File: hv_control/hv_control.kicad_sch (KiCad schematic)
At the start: 158 parts, among them J1 DB9, J10 x, J11 Conn_02x03_Odd_Even, J12 x, J13 Conn_01x02_Male, J14 Conn_01x02_Male, J15 Conn_01x02_Male, J16 Conn_01x02_Male, J17 Conn_01x02_Male, J2 DB15, J3 INPUTS, J4 I/O, J5 USB_B_Mini, J6 Conn_01x01_Male, J7 Conn_01x01_Male, J8 Conn_02x04_Odd_Even, J9 x, K1 RELAY_DPDT, K2 RELAY_DPDT, P2 SWD, P8 CONN_01X01, Q2 BSS138, Q3 BSS138, U1 XMC4400-F100, U10 XMC1301T016F0032ABXUMA1, U11 LT1764EQ, U12 LMV331, U13 DRV8870DDA, U14 AD8226, U15 MAX3463, U18 LT1764EQ, U19 KSZ8081, U2 ips511g, U20 ETH100_MAG, U21 MAX3463, U22 MAX3463, U23 MAX3463, U3 ips511g, U4 MAX3463, U5 AD8226, U6 R-78E5.0-0.5, U7 TS321, U8 R-78E3.3-0.5, U9 ISO7321C, Y1 12MHz, Y2 25MHz

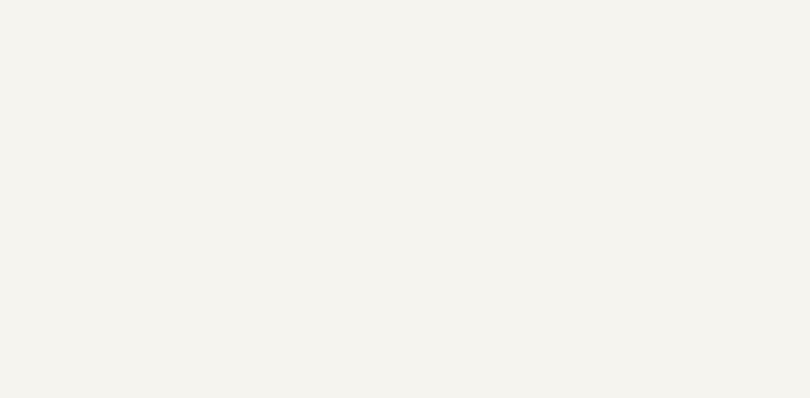
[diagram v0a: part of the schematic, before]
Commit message: Initial xmc1300 code.
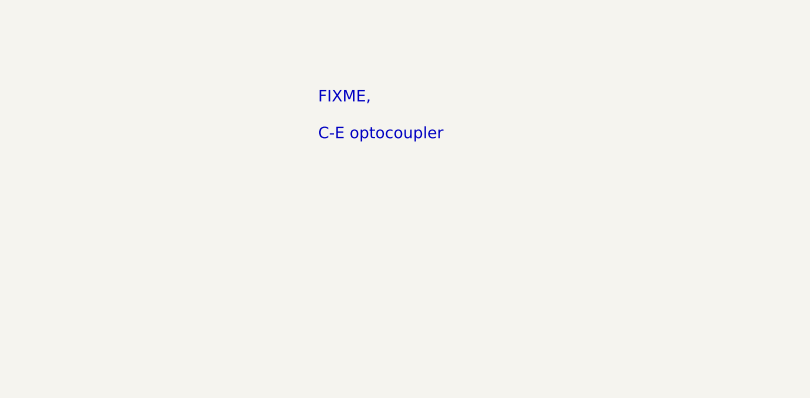
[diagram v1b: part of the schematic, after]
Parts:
- Y2: Mouser (none) -> 581-CX3225CA25000PPQ
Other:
- note added: "FIXME, C-E optocoupler"
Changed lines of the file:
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@@
     (effects (font (size 1.27 1.27)) (justify right bottom))
   )
+  (text "FIXME,\n\nC-E optocoupler" (at 400.05 29.21 0)
+    (effects (font (size 1.27 1.27)) (justify left bottom))
+  )
   (label "VddC" (at 45.72 370.84 0)
     (effects (font (size 1.524 1.524)) (justify left bottom))
@@
       (effects (font (size 1.27 1.27)) hide)
     )
+    (property "Mouser" " 581-CX3225CA25000PPQ " (id 8) (at 203.2 130.81 0)
+      (effects (font (size 1.27 1.27)) hide)
+    )

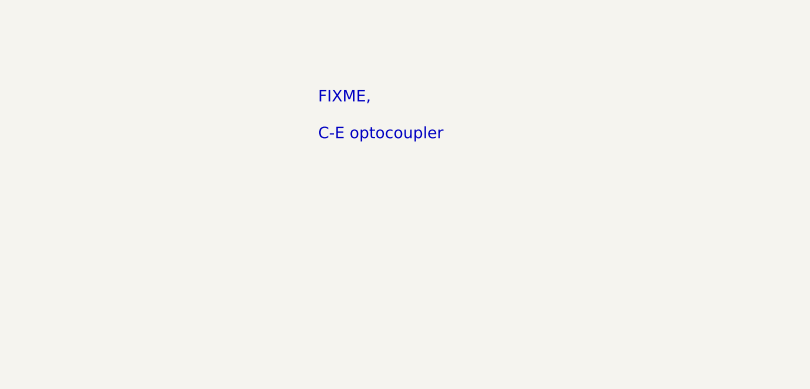
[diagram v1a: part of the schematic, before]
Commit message: xmc1300 can toggle pin.
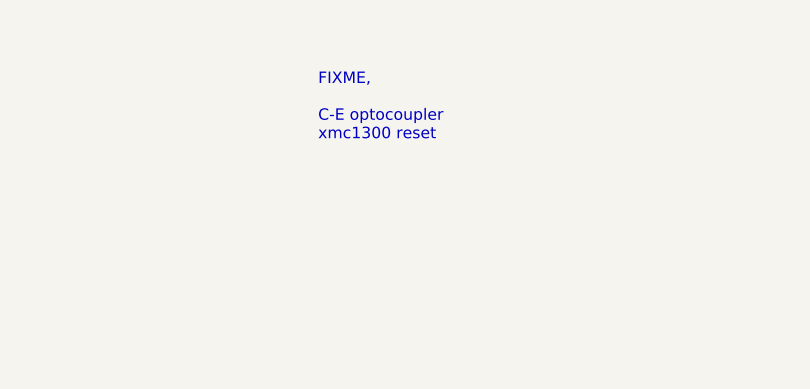
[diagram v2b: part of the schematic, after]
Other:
- note added: "FIXME, C-E optocoupler xmc1300 reset"
- note removed: "FIXME, C-E optocoupler"
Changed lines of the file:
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@@
     (effects (font (size 1.27 1.27)) (justify right bottom))
   )
-  (text "FIXME,\n\nC-E optocoupler" (at 400.05 29.21 0)
+  (text "FIXME,\n\nC-E optocoupler\nxmc1300 reset" (at 400.05 29.21 0)
     (effects (font (size 1.27 1.27)) (justify left bottom))
   )

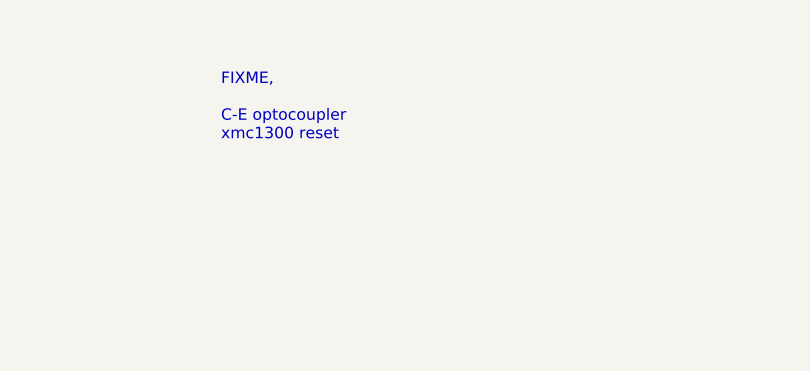
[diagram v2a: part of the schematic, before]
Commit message: Adding scripts to use the parallel trace port. Only 4-bit interface tested.
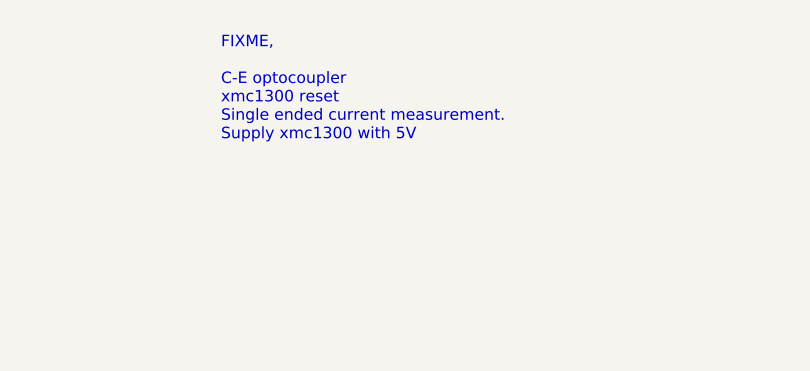
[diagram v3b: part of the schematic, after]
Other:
- note added: "FIXME, C-E optocoupler xmc1300 reset Single ended current measurement. Supply xmc1300 with 5V"
- note removed: "FIXME, C-E optocoupler xmc1300 reset"
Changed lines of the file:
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@@
     (effects (font (size 1.27 1.27)) (justify right bottom))
   )
-  (text "FIXME,\n\nC-E optocoupler\nxmc1300 reset" (at 400.05 29.21 0)
+  (text "FIXME,\n\nC-E optocoupler\nxmc1300 reset\nSingle ended current measurement.\nSupply xmc1300 with 5V"
+    (at 400.05 29.21 0)
     (effects (font (size 1.27 1.27)) (justify left bottom))
   )

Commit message: Moving to new CCU8 implementation. Moved trace and @arm scripts to octave archive.
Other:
- note added: "FIXME, C-E optocoupler xmc1300 reset Single ended current measurement. Supply xmc1300 with 5V Add connector for GNDPWR busbar"
- note removed: "FIXME, C-E optocoupler xmc1300 reset Single ended current measurement. Supply xmc1300 with 5V"
